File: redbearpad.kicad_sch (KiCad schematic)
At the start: 11 parts, among them J1 BlendMicro_fila_izq, J2 BlendMicro_fila_der, J3 OLED_128x32_I2C, SW1 Redragon_LP, SW2 Redragon_LP, SW3 Redragon_LP, SW4 Redragon_LP, SW5 Redragon_LP, SW6 Redragon_LP, SW7 Redragon_LP, SW8 Redragon_LP

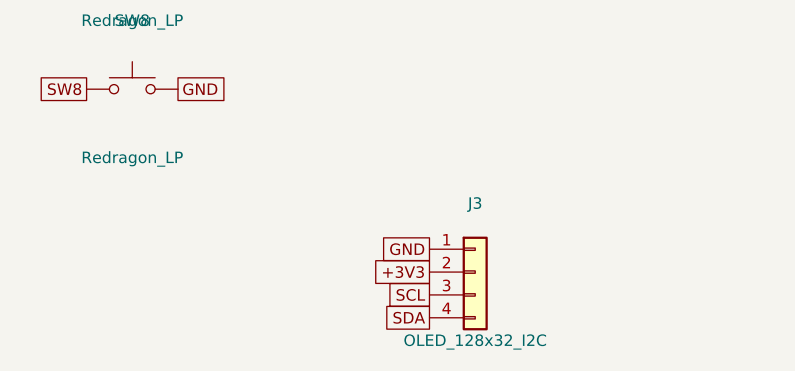
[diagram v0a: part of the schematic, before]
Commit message: Corregir orden de pines OLED a SDA/SCL/VCC/GND segun ajuste fisico del modulo
- J3 reordenado en gen_sch.py y verify_netlist.py
- Reruteo de SDA/SCL/+3V3 a las nuevas posiciones de pad; SCL despeja el pad +3V3
- Serigrafia OLED invertida; renders y gerbers regenerados; spec actualizado
- DRC 0 violaciones / 0 unconnected, ERC 0, netlist OK

Co-Authored-By: Claude Fable 5 <noreply@anthropic.com>
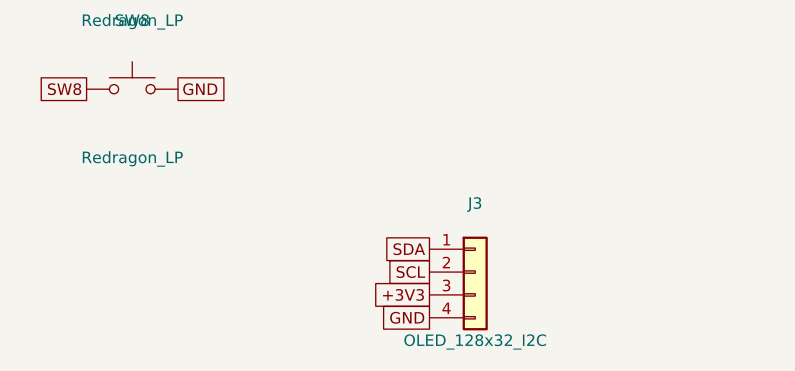
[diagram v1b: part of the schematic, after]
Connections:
- net +3V3: now also J3.3 (Pin_3); no longer J3.2 (Pin_2)
- net GND: now also J3.4 (Pin_4); no longer J3.1 (Pin_1)
- net SCL: now also J3.2 (Pin_2); no longer J3.3 (Pin_3)
- net SDA: now also J3.1 (Pin_1); no longer J3.4 (Pin_4)
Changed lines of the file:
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@@
     (instances (project "redbearpad" (path "/f0a11111-2222-3333-4444-555566667777" (reference "J3") (unit 1))))
   )
-  (global_label "GND" (shape passive) (at 96.52 149.86 180) (effects (font (size 1.27 1.27)) (justify right)))
-  (global_label "+3V3" (shape passive) (at 96.52 152.4 180) (effects (font (size 1.27 1.27)) (justify right)))
-  (global_label "SCL" (shape passive) (at 96.52 154.94 180) (effects (font (size 1.27 1.27)) (justify right)))
-  (global_label "SDA" (shape passive) (at 96.52 157.48000000000002 180) (effects (font (size 1.27 1.27)) (justify right)))
+  (global_label "SDA" (shape passive) (at 96.52 149.86 180) (effects (font (size 1.27 1.27)) (justify right)))
+  (global_label "SCL" (shape passive) (at 96.52 152.4 180) (effects (font (size 1.27 1.27)) (justify right)))
+  (global_label "+3V3" (shape passive) (at 96.52 154.94 180) (effects (font (size 1.27 1.27)) (justify right)))
+  (global_label "GND" (shape passive) (at 96.52 157.48000000000002 180) (effects (font (size 1.27 1.27)) (justify right)))
   (sheet_instances (path "/" (page "1")))
 )
